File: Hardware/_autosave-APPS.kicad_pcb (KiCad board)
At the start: 2 copper layers, 100 x 75 mm, 81 parts, among them J4 Sygnały, J5 Diagnostyka, J8 Zasilanie+CAN, K1 FINDER-30.22, Q1 BSS138, SW1 SW_Push, U1 STM32L4P5RET6, U2 LM2596S-5, U3 LM1117-3.3, U4 LM1117-3.3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

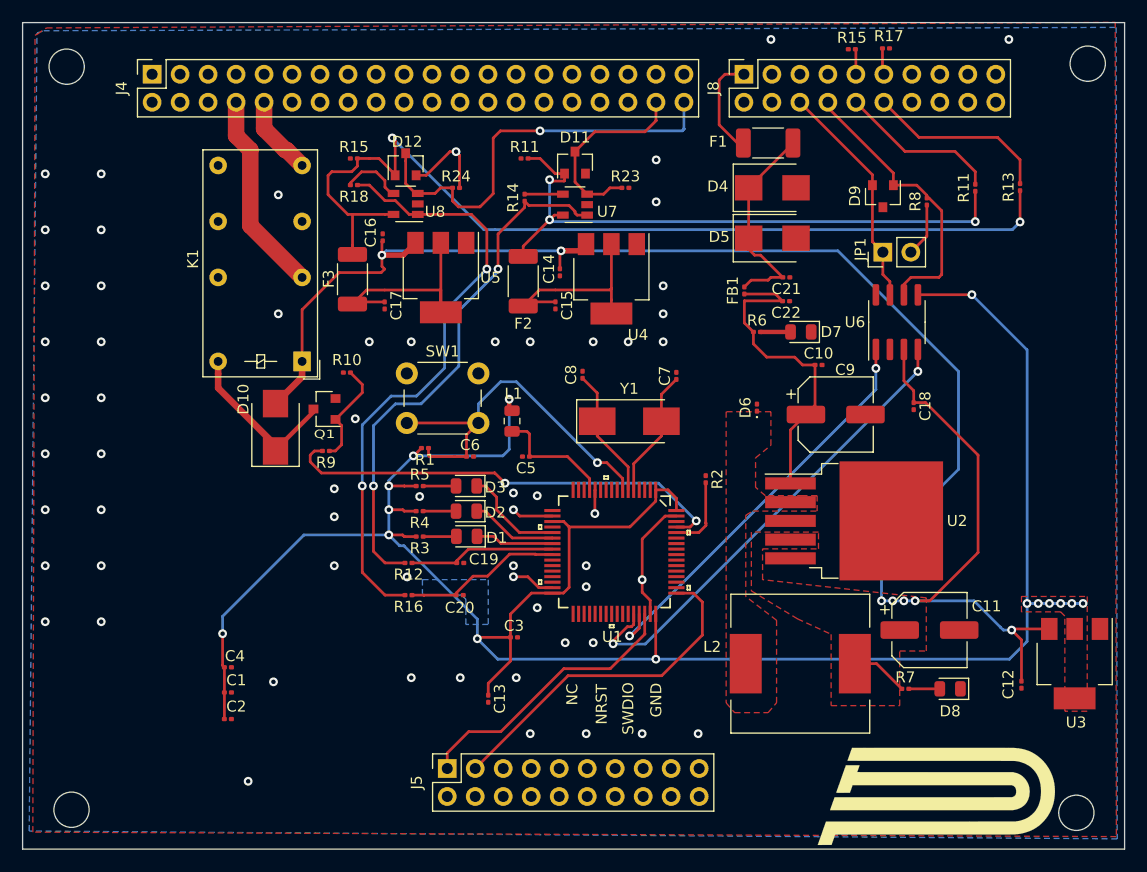
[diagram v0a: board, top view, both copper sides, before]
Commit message: Changed footprints and PCB layout. Schematic cleanup.
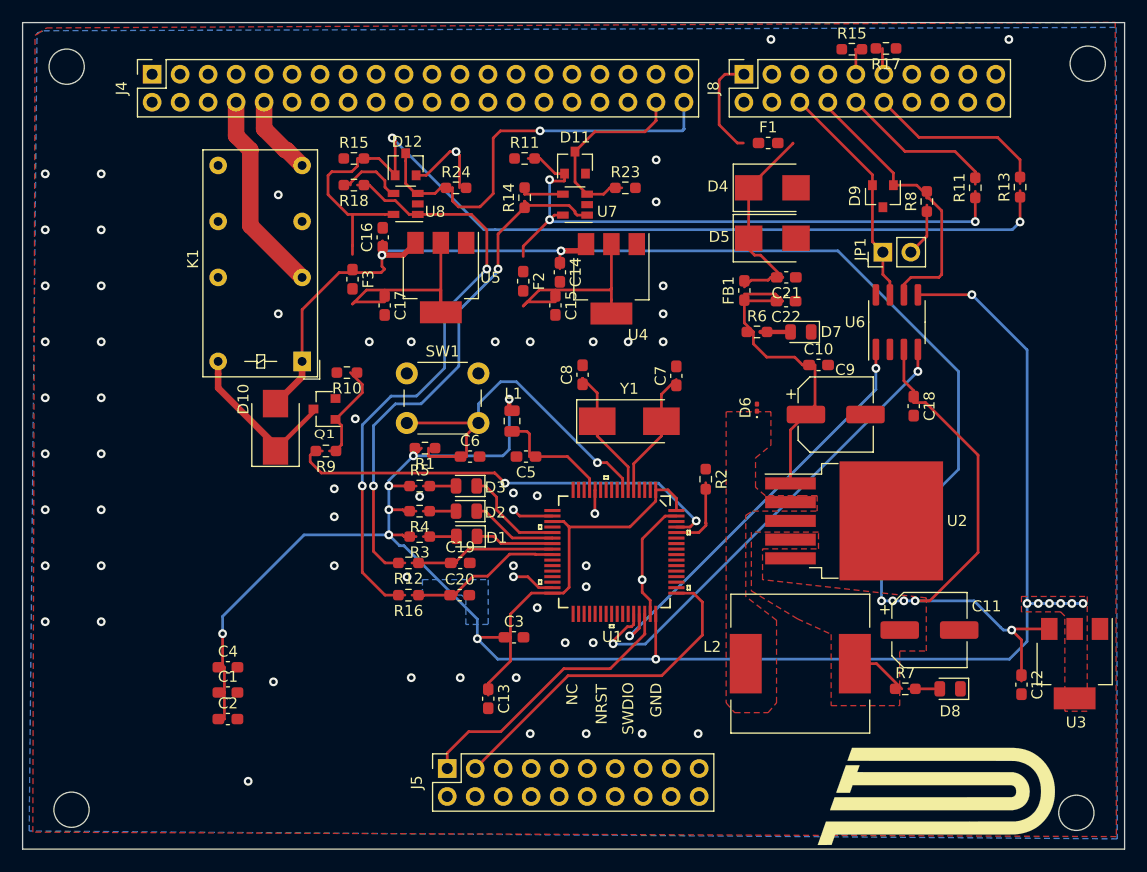
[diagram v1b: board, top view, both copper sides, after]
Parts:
- C1, C10, C12, C13, C14, C15, C16, C17, C18, C19, C2, C20, C21, C22, C3, C4, C5, C6, C7, C8: footprint Capacitor_SMD:C_0201_0603Metric -> Capacitor_SMD:C_0603_1608Metric_Pad1.08x0.95mm_HandSolder
- F1, F2, F3: footprint Fuse:Fuse_2010_5025Metric -> Fuse:Fuse_0603_1608Metric_Pad1.05x0.95mm_HandSolder
- FB1: footprint Inductor_SMD:L_0201_0603Metric -> Inductor_SMD:L_0603_1608Metric_Pad1.05x0.95mm_HandSolder
- R1, R10, R11 (x2), R12, R13, R14, R15 (x2), R16, R17, R18, R2, R23, R24, R3, R4, R5, R6, R7, R8, R9: footprint Resistor_SMD:R_0201_0603Metric -> Resistor_SMD:R_0603_1608Metric_Pad0.98x0.95mm_HandSolder
